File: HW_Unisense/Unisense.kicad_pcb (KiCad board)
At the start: 2 copper layers, 76.2 x 73.1 mm, 95 parts, among them J10 OneWire, J2 SW1, J3 SW2, J4 GeigerCounter, J5 WS2812, J6 LED1, J7 LED2, J8 LED3, J9 RS485, P1 SM02B-NSHSS-TB(LF)(SN), Q1 BSN20, Q2 BSN20, Q3 BSN20, Q4 BSN20, Q5 AO3400A, Q6 AO3400A, Q7 AO3400A, Q8 IRLML6402TRPBF, SW1 K2-1102SP-C4SC-04, SW2 K2-1102SP-C4SC-04, SW3 K2-1102SP-C4SC-04, SW4 K2-1102SP-C4SC-04, U1 ESP32-S3-WROOM-1(N8R2), U11 PCF85263ATT, U2 S4B-PH-SM4-K-TB(LF)(SN), U3 LD1117S33TR, U4 TMP112xxDRL, U5 BME280, U6 BMP280, U7 VEML6040A3OG, U8 MCP73831T-2ATI/OT, U9 MAX17048G+T10, Y1 Crystal

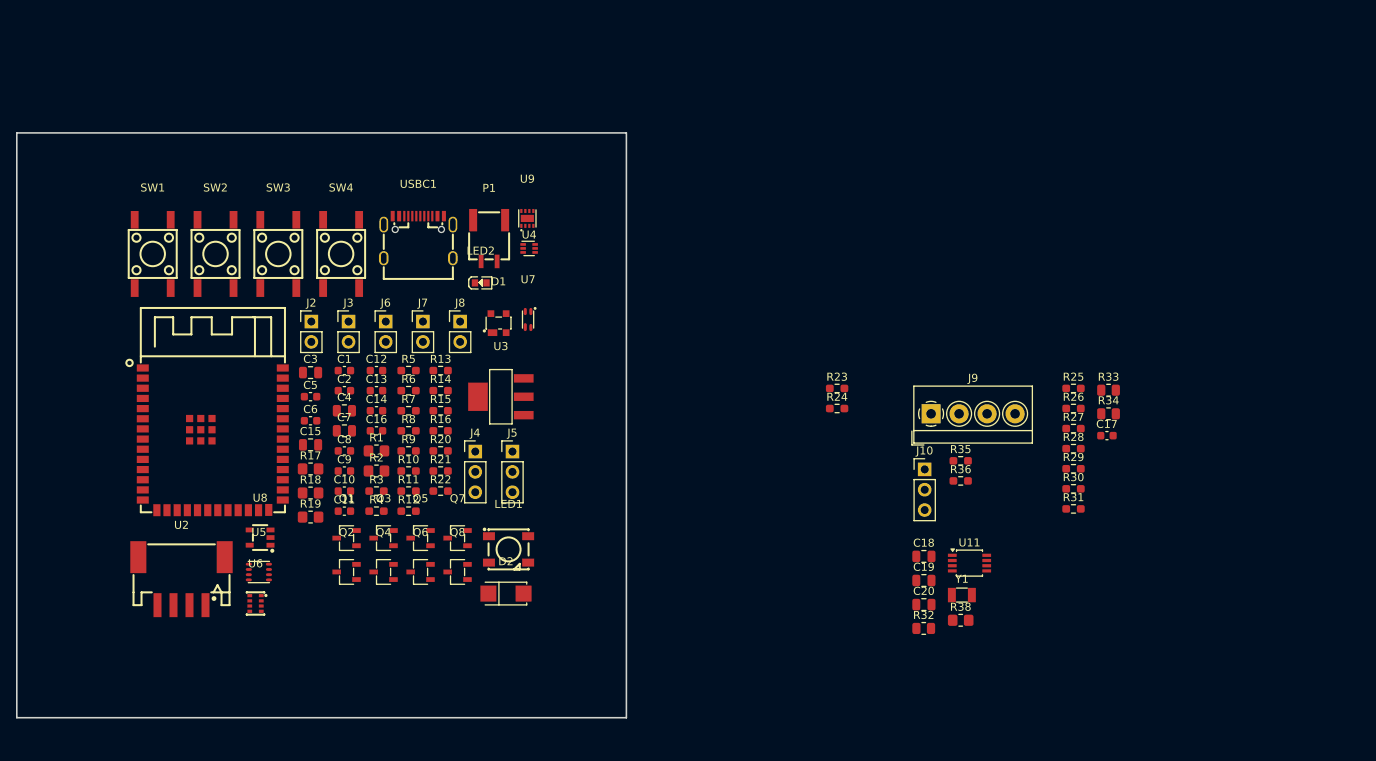
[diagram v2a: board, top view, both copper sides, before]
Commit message: add mor sensors, place parts
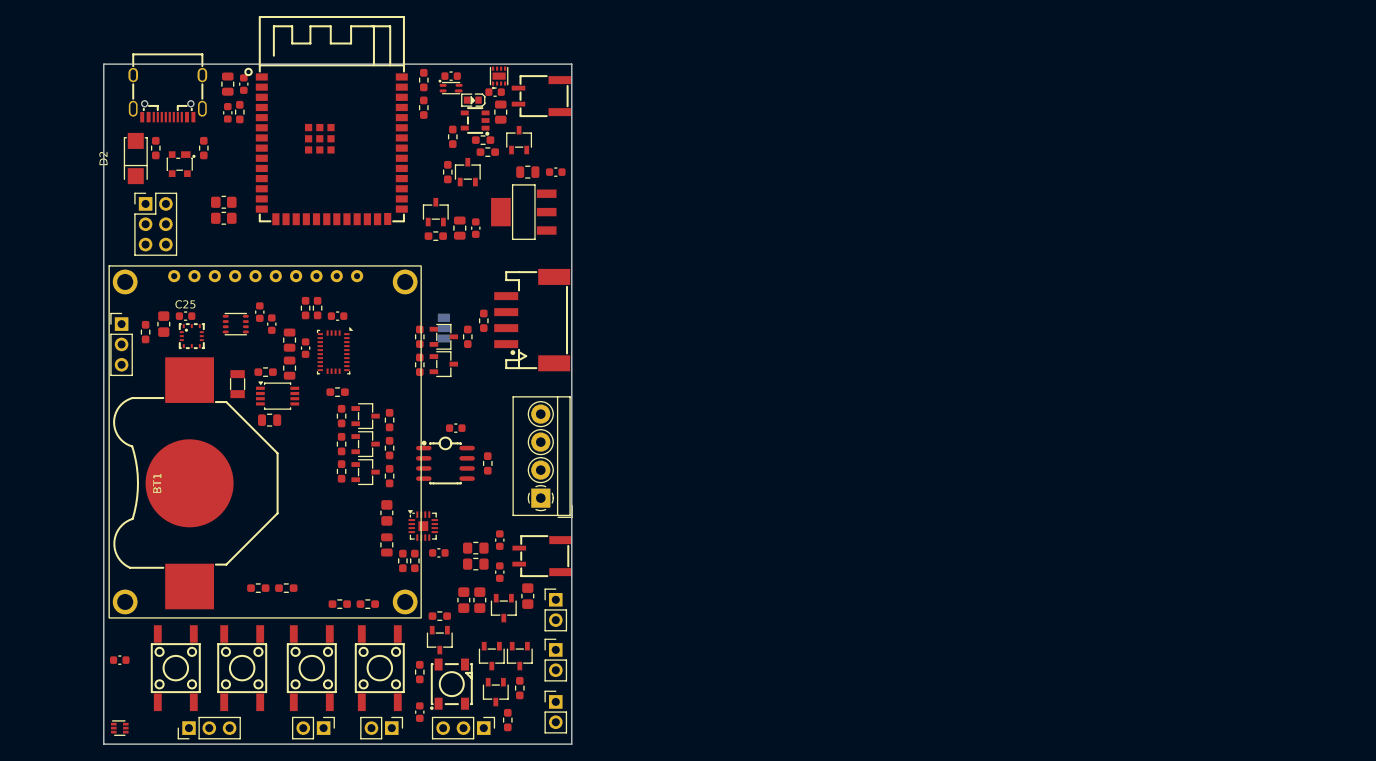
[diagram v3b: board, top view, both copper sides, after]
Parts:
- added BT1: Battery_Cell, burgerLibFP:BAT-SMD_MYOUNG_MY-2032-04, F.Cu at (131.0, 103.4)
- added C21: 10u, Capacitor_SMD:C_0805_2012Metric, F.Cu at (155.7, 111.1)
- added C22: 100n, Capacitor_SMD:C_0603_1608Metric, F.Cu at (162.2, 112.1)
- added C23: 220pF, Capacitor_SMD:C_0603_1608Metric, F.Cu at (169.8, 110.5)
- added C24: 220pF, Capacitor_SMD:C_0603_1608Metric, F.Cu at (169.8, 114.5)
- added C25: 100n, Capacitor_SMD:C_0603_1608Metric, F.Cu at (130.5, 82.5)
- added FB1: FerriteBead, Inductor_SMD:L_0805_2012Metric_Pad1.15x1.40mm_HandSolder, F.Cu at (166.8, 113.5)
- added FB2: FerriteBead, Inductor_SMD:L_0805_2012Metric_Pad1.15x1.40mm_HandSolder, F.Cu at (166.8, 111.5)
- added J1: Conn_02x03_Odd_Even, Connector_PinHeader_2.54mm:PinHeader_2x03_P2.54mm_Vertical, F.Cu at (125.5, 68.5)
- added JP1: SolderJumper_3_Open, Jumper:SolderJumper-3_P1.3mm_Open_Pad1.0x1.5mm, B.Cu at (162.8, 84.0)
- added P2: SM02B-NSHSS-TB(LF)(SN), burgerLibFP:CONN-SMD_SM02B-NSHSS-TB-LF-SN, F.Cu at (174.8, 112.5)
- added Q10: IRLML6402TRPBF, EduboardV2_kicadlib:SOT-23-3_L2.9-W1.6-P1.90-LS2.8-BR, F.Cu at (161.8, 69.5)
- added Q11: BSN20, EduboardV2_kicadlib:SOT-23-3_L2.9-W1.6-P1.90-LS2.8-BR, F.Cu at (153.0, 102.0)
- added Q12: BSN20, EduboardV2_kicadlib:SOT-23-3_L2.9-W1.6-P1.90-LS2.8-BR, F.Cu at (153.0, 98.5)
- added Q13: BSN20, EduboardV2_kicadlib:SOT-23-3_L2.9-W1.6-P1.90-LS2.8-BR, F.Cu at (153.0, 95.0)
- added Q9: IRLML6402TRPBF, EduboardV2_kicadlib:SOT-23-3_L2.9-W1.6-P1.90-LS2.8-BR, F.Cu at (165.8, 64.5)
- added R37: 10k, Resistor_SMD:R_0603_1608Metric_Pad0.98x0.95mm_HandSolder, F.Cu at (147.0, 81.5)
- added R39: 10k, Resistor_SMD:R_0603_1608Metric_Pad0.98x0.95mm_HandSolder, F.Cu at (145.5, 81.5)
- added R40: 10k, Resistor_SMD:R_0603_1608Metric_Pad0.98x0.95mm_HandSolder, F.Cu at (149.5, 92.0)
- added R41: 100k, Resistor_SMD:R_0603_1608Metric_Pad0.98x0.95mm_HandSolder, F.Cu at (159.2, 113.1)
- added R42: 100k, Resistor_SMD:R_0603_1608Metric_Pad0.98x0.95mm_HandSolder, F.Cu at (157.7, 113.1)
- added R43: 0R, Resistor_SMD:R_0805_2012Metric_Pad1.20x1.40mm_HandSolder, F.Cu at (155.7, 107.1)
- added U10: SP3485EN-L/TR, EduboardV2_kicadlib:SOIC-8_L5.0-W4.0-P1.27-LS6.0-BL, F.Cu at (163.0, 100.9)
- added U12: MAX98357A, Package_DFN_QFN:TQFN-16-1EP_3x3mm_P0.5mm_EP1.23x1.23mm, F.Cu at (160.2, 108.8)
- added U13: ZMOD4510AI1R, burgerLibFP:LGA-12_L3.0-W3.0-P0.50-BL_ZMOD4410AI1V, F.Cu at (131.3, 85.0)
- added X1: ~, burgerLibFP:DFR0649, F.Cu at (140.6, 95.8)
- R32, R33, R34: footprint Resistor_SMD:R_0805_2012Metric -> Resistor_SMD:R_0603_1608Metric_Pad0.98x0.95mm_HandSolder
- U6: value BMP280 -> BNO055; footprint burgerLibFP:LGA-8_L2.5-W2.0-P0.65_AMP6127 -> Package_LGA:LGA-28_5.2x3.8mm_P0.5mm
- moved R38 106.3 mm to (127.8, 83.5), turned to 90 degrees
- moved R36 103.6 mm to (125.5, 84.5), turned to 90 degrees
- moved J10 102.0 mm to (122.5, 83.5)
- moved Y1 94.3 mm to (137.0, 91.0), turned to 90 degrees
- moved R33 94.0 mm to (160.3, 53.0), turned to -90 degrees
- moved R34 93.8 mm to (160.3, 56.5), turned to 90 degrees
- moved R30 91.9 mm to (150.0, 95.0), turned to 90 degrees
- moved R26 91.8 mm to (150.0, 101.9), turned to 90 degrees
- moved R28 91.5 mm to (150.0, 98.5), turned to 90 degrees
- moved U11 89.0 mm to (142.0, 92.5)
- moved R32 88.3 mm to (140.5, 89.5), turned to 180 degrees
- moved R31 86.2 mm to (156.0, 95.5), turned to -90 degrees
- moved R35 85.8 mm to (143.1, 116.5), turned to 180 degrees
- moved R27 85.7 mm to (156.0, 102.5), turned to -90 degrees
- moved R29 85.5 mm to (156.0, 99.0), turned to -90 degrees
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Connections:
- net VBUS renamed V_USB
- net Vdrive renamed +5V_SW
- C10 pad 1: Net-(U6-VDD) -> +3.3V_SW
- C11 pad 1: Net-(U6-VDD) -> Net-(U6-CAP)
- C12 pad 1: +VSW -> +3.3V_SW
- C13 pad 1: +VSW -> +3.3V_SW
- C14 pad 2: +VSW -> +3.3V_SW
- C18 pad 1: +VSW -> +3.3V_SW
- C19 pad 1: +VSW -> +3.3V_SW
- C9 pad 1: +VSW -> +3.3V_SW
- J10 pad 1: +VSW -> +3.3V_SW
- Q1 pad 1: +VSW -> +3.3V_SW
- Q2 pad 1: +VSW -> +3.3V_SW
- Q3 pad 1: +VSW -> +3.3V_SW
- Q4 pad 1: +VSW -> +3.3V_SW
- R10 pad 2: +VSW -> +3.3V_SW
- R13 pad 2: +VSW -> +3.3V_SW
- R26 pad 2: +VSW -> +3.3V_SW
- R28 pad 2: +VSW -> +3.3V_SW
- R30 pad 2: +VSW -> +3.3V_SW
- R36 pad 2: +VSW -> +3.3V_SW
- R38 pad 2: +VSW -> +3.3V_SW
- R6 pad 2: +VSW -> +3.3V_SW
- R7 pad 2: +VSW -> +3.3V_SW
- U11 pad 8: +VSW -> +3.3V_SW
- U4 pad 5: +VSW -> +3.3V_SW
- U5 pad 2: +VSW -> +3.3V_SW
- U5 pad 6: +VSW -> +3.3V_SW
- U5 pad 8: +VSW -> +3.3V_SW
- U6 pad 1: GND -> unconnected-(U6-PIN1-Pad1)
- U6 pad 2: +VSW -> GND
- U6 pad 3: SDA -> +3.3V_SW
- U6 pad 4: SCL -> +3.3V_SW
- U6 pad 5: GND -> Net-(U6-PS1)
- U6 pad 6: Net-(U6-VDD) -> Net-(U6-PS0)
- U6 pad 7: GND -> unconnected-(U6-PIN7-Pad7)
- U6 pad 8: Net-(U6-VDD) -> unconnected-(U6-PIN8-Pad8)
- U7 pad 4: +VSW -> +3.3V_SW
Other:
- board size 76.2 x 73.1 mm -> 58.5 x 85 mm
